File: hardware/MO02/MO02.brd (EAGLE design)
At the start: 49 x 24.5 mm, 33 parts, among them J1 AUDIO-JACK2PTH, J2 M04X2, Q1 G2XX3---PW20, Q4 32.768 kHz, SW1 DTS-6

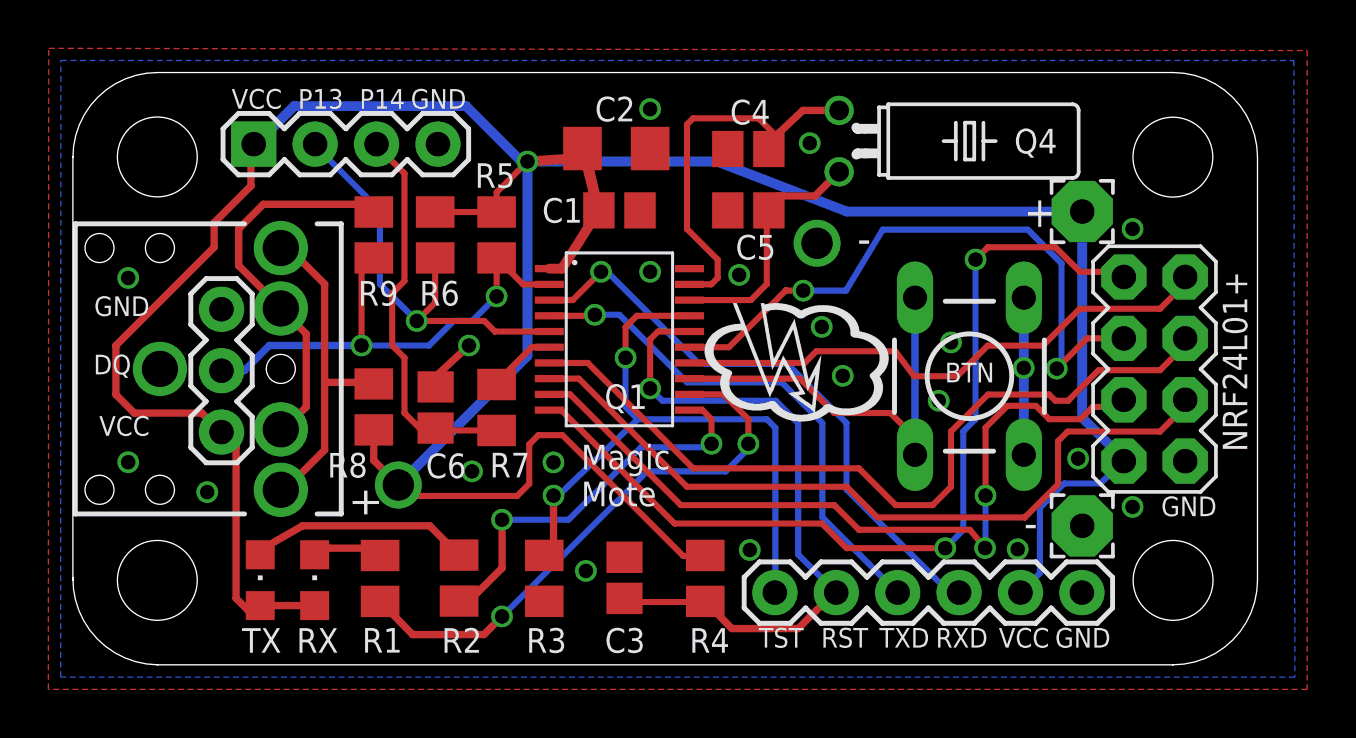
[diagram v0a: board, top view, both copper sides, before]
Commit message: 2x6mm watch crystal, isolated ground plane, no external caps
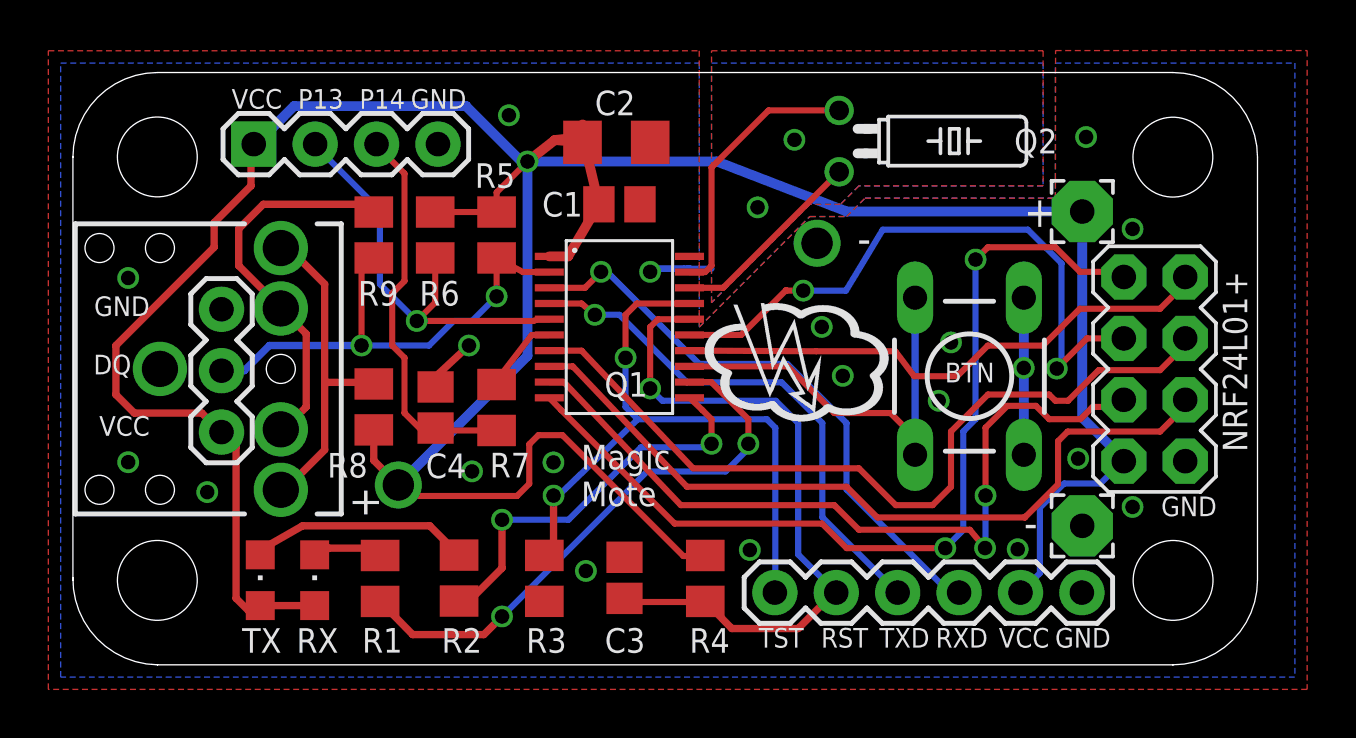
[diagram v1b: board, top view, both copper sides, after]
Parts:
- removed C5: 12nF, resistor:C0805
- removed C6: 330nF, resistor:C0805
- removed Q4: 32.768 kHz, crystal:TC38H
- added Q2: 32.768 kHz, crystal:TC26H
- C4: value 12nF -> 330nF
- moved C4 16.8 mm to (15.0, 10.6), turned to 90 degrees
- moved Q1 0.51 mm to (22.6, 14.0)
- moved C1 0.25 mm to (22.6, 19.1)
- moved C2 0.25 mm to (22.5, 21.6)
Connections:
- net GND: no longer C5.2, C6.2
- net N$7: now also C4.1; no longer C6.1
- net P2.6: now also Q2.1; no longer C4.1, Q4.1
- net P2.7: now also Q2.2; no longer C5.1, Q4.2
- net RXD: now also J4.4, Q1.3; no longer J4.3, Q1.4
- net TXD: now also J4.3, Q1.4; no longer J4.4, Q1.3
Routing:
- net P2.6: track 15.9 -> 11.3 mm
- net GND: track 8.87 -> 13.0 mm, vias 21 -> 22
- net TXD: track 24.5 -> 21.6 mm
- net +3V3: track 137.9 -> 135.1 mm
- net RXD: track 21.9 -> 24.3 mm
- net P2.7: track 10.2 -> 8.18 mm
- net RST: track 28.1 -> 28.6 mm
- net TST: track 27.3 -> 27.8 mm

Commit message: removed pulldown resistor on TST
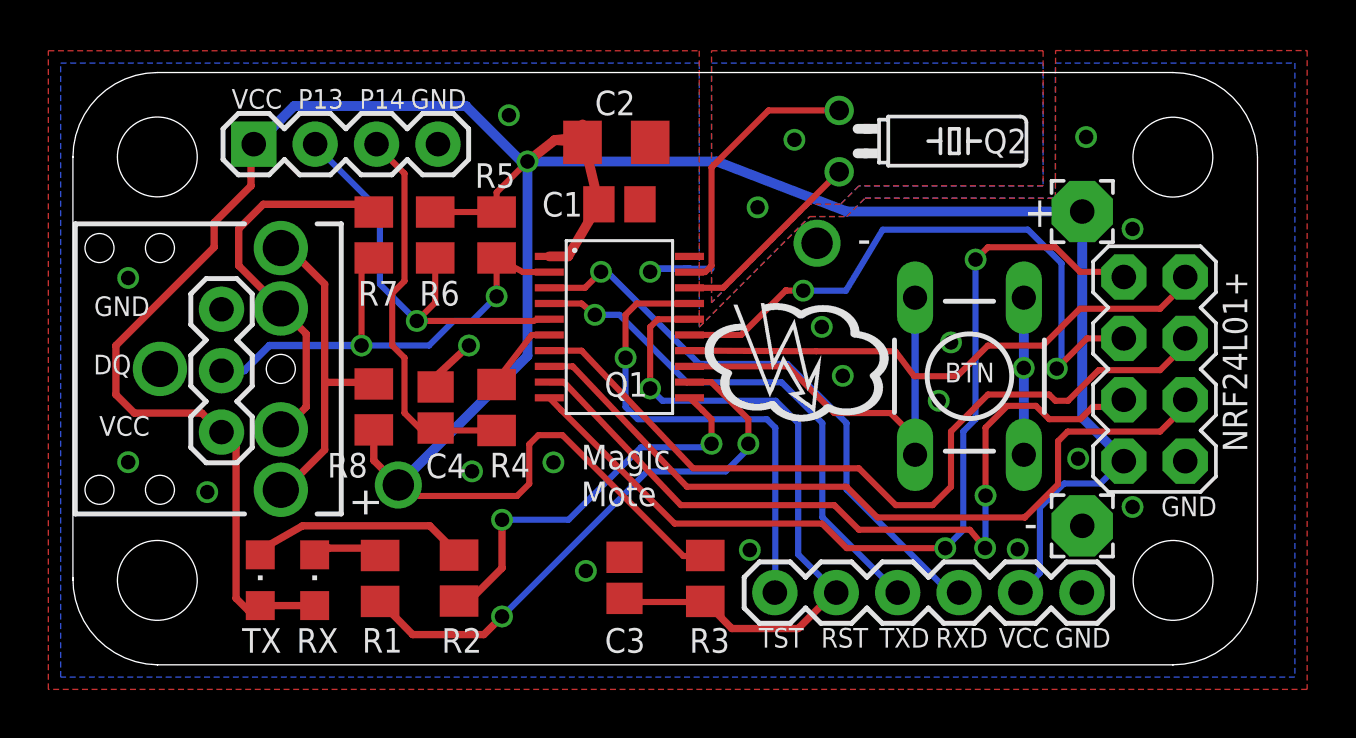
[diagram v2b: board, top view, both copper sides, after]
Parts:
- removed R9: 220R, resistor:M0805
- R4: value 47K -> 10K
- R7: value 10K -> 220R
- moved R4 11.2 mm to (17.5, 10.6), turned to 90 degrees
- moved R7 8.76 mm to (12.4, 17.8)
- moved R3 6.66 mm to (26.2, 3.57)
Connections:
- net +3V3: now also R3.1; no longer R4.1
- net DQ: now also R7.1; no longer R9.1
- net GND: no longer R3.2
- net N$4: now also R7.2; no longer R9.2
- net N$7: now also R4.1; no longer R7.1
- net P1.4: now also R4.2; no longer R7.2
- net RST: now also R3.2; no longer R4.2
- net TST: no longer R3.1
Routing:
- net TST: track 27.8 -> 20.0 mm, vias 2 -> 1
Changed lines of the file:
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@@
 <attribute name="MF" value="" x="31.695" y="21.663" size="1.778" layer="27" rot="R270" display="off"/>
 <attribute name="OC_FARNELL" value="unknown" x="31.695" y="21.663" size="1.778" layer="27" rot="R270" display="off"/>
-<attribute name="NAME" x="38.934" y="21.155" size="1.016" layer="25" font="vector" ratio="15"/>
+<attribute name="NAME" x="37.664" y="21.155" size="1.016" layer="25" font="vector" ratio="15"/>
 </element>
 <element name="J3" library="SparkFun" package="1X04" value="" x="7.4796" y="21.537" smashed="yes"/>
@@
 <attribute name="NAME" x="22" y="0.5" size="1.016" layer="25" font="vector" ratio="15"/>
 </element>
-<element name="R4" library="resistor" package="M0805" value="47K" x="26.158" y="3.5734" smashed="yes" rot="R270">
+<element name="R3" library="resistor" package="M0805" value="47K" x="26.158" y="3.5734" smashed="yes" rot="R270">
 <attribute name="RESISTANCE" value="4K7" x="26.158" y="3.5734" size="1.778" layer="27" rot="R270" display="off"/>
 <attribute name="NAME" x="25.5" y="0.5" size="1.016" layer="25" font="vector" ratio="15"/>
@@
 <element name="U$4" library="SparkFun" package="STAND-OFF" value="" x="3.492" y="21.008"/>
 <element name="U$5" library="SparkFun" package="STAND-OFF" value="" x="45.5" y="21" smashed="yes"/>
-<element name="R3" library="resistor" package="M0805" value="47K" x="19.5" y="3.5762" smashed="yes" rot="R270">
-<attribute name="RESISTANCE" value="4K7" x="19.5" y="3.5762" size="1.778" layer="27" rot="R270" display="off"/>
-<attribute name="NAME" x="18.75" y="0.5" size="1.016" layer="25" ratio="15"/>
-</element>
 <element name="-" library="wirepad" package="2,54/1,0" value="" x="41.75" y="5.75" smashed="yes">
 <attribute name="NAME" x="39.337" y="5.242" size="1.27" layer="25" ratio="15"/>
@@
 <attribute name="NAME" x="16.272" y="8.739" size="1.016" layer="25" font="vector" ratio="15" rot="R180"/>
 </element>
-<element name="R7" library="resistor" package="M0805" value="10K" x="17.526" y="10.644" smashed="yes" rot="R90">
+<element name="R4" library="resistor" package="M0805" value="10K" x="17.526" y="10.644" smashed="yes" rot="R90">
 <attribute name="RESISTANCE" value="4K7" x="17.526" y="10.644" size="1.778" layer="27" rot="R90" display="off"/>
 <attribute name="NAME" x="18.913" y="8.77" size="1.016" layer="25" font="vector" ratio="15" rot="R180"/>
@@
 <attribute name="NAME" x="12.192" y="8.763" size="1.016" layer="25" ratio="15" rot="R180"/>
 </element>
-<element name="R9" library="resistor" package="M0805" value="220R" x="12.446" y="17.78" smashed="yes" rot="R90">
+<element name="R7" library="resistor" package="M0805" value="220R" x="12.446" y="17.78" smashed="yes" rot="R90">
 <attribute name="RESISTANCE" value="4K7" x="12.446" y="17.78" size="1.778" layer="27" rot="R90" display="off"/>
 <attribute name="NAME" x="13.462" y="15.875" size="1.016" layer="25" ratio="15" rot="R180"/>
@@
 <contactref element="R5" pad="2"/>
 <contactref element="Q1" pad="2"/>
-<contactref element="R9" pad="1"/>
+<contactref element="R7" pad="1"/>
 <contactref element="J5" pad="2"/>
 <wire x1="19.7059" y1="16.2449" x2="18.6191" y2="16.2449" width="0.254" layer="1"/>
@@
 <contactref element="J2" pad="2"/>
 <contactref element="J3" pad="1"/>
-<contactref element="R4" pad="1"/>
+<contactref element="R3" pad="1"/>
 <contactref element="J4" pad="5"/>
 <contactref element="R6" pad="1"/>
@@
 <contactref element="Q1" pad="16"/>
 <contactref element="J4" pad="2"/>
-<contactref element="R4" pad="2"/>
+<contactref element="R3" pad="2"/>
 <contactref element="C3" pad="1"/>
 <wire x1="25.506" y1="14.295" x2="24.201" y2="14.295" width="0.254" layer="1"/>
@@
 <contactref element="Q1" pad="17"/>
 <contactref element="J4" pad="1"/>
-<contactref element="R3" pad="1"/>
 <wire x1="25.506" y1="14.945" x2="23.327" y2="14.945" width="0.254" layer="1"/>
 <wire x1="23.327" y1="14.945" x2="22.86" y2="14.478" width="0.254" layer="1"/>
@@
 <wire x1="29.0562" y1="9.8058" x2="29.0562" y2="3.0072" width="0.254" layer="16"/>
 <wire x1="29.0562" y1="3.0072" x2="29.0362" y2="2.9872" width="0.254" layer="16"/>
-<wire x1="19.5" y1="4.5262" x2="19.5122" y2="4.5262" width="0.3048" layer="1"/>
-<wire x1="19.5122" y1="4.5262" x2="19.812" y2="4.826" width="0.3048" layer="1"/>
-<via x="19.881" y="7" extent="1-16" drill="0.6" shape="square" alwaysstop="yes"/>
-<wire x1="19.881" y1="7" x2="20.081" y2="7" width="0.254" layer="16"/>
-<wire x1="20.081" y1="7" x2="23.368" y2="10.16" width="0.254" layer="16"/>
+<wire x1="19.881" y1="7" x2="20.081" y2="7" width="0" layer="19" extent="1-16"/>
+<wire x1="20.081" y1="7" x2="23.368" y2="10.16" width="0" layer="19" extent="1-16"/>
 <wire x1="22.86" y1="10.668" x2="23.368" y2="10.16" width="0.254" layer="16"/>
-<wire x1="19.881" y1="7" x2="19.881" y2="5.0342" width="0.3048" layer="1"/>
-<wire x1="19.881" y1="5.0342" x2="19.5" y2="4.5262" width="0.3048" layer="1"/>
+<wire x1="19.881" y1="7" x2="19.881" y2="5.0342" width="0" layer="19" extent="1-16"/>
 </signal>
 <signal name="TXD">
@@
 <signal name="P1.4">
 <contactref element="Q1" pad="6"/>
-<contactref element="R7" pad="2"/>
+<contactref element="R4" pad="2"/>
 <wire x1="19.7059" y1="13.645" x2="18.979" y2="13.645" width="0.254" layer="1"/>
 <wire x1="18.979" y1="13.645" x2="17.272" y2="11.43" width="0.254" layer="1"/>
@@
 <vertex x="-0.508" y="-0.508"/>
 </polygon>
-<contactref element="R3" pad="2"/>
 <via x="2.286" y="8.382" extent="1-16" drill="0.6" shape="square" alwaysstop="yes"/>
 <via x="2.286" y="16.002" extent="1-16" drill="0.6" shape="square" alwaysstop="yes"/>
@@
 <wire x1="24.0069" y1="16.3869" x2="24.003" y2="16.383" width="0.254" layer="16"/>
 <wire x1="24.003" y1="16.383" x2="23.876" y2="16.256" width="0.254" layer="16"/>
+<wire x1="43.831" y1="18.03" x2="41.91" y2="21.832" width="0" layer="19" extent="1-1"/>
+<wire x1="39.334" y1="15.188" x2="43.831" y2="18.03" width="0" layer="19" extent="1-1"/>
+<wire x1="41.581" y1="8.53" x2="39.37" y2="8.652" width="0" layer="19" extent="16-16"/>
+<wire x1="41.75" y1="5.75" x2="41.581" y2="8.53" width="0" layer="19" extent="1-1"/>
+<wire x1="43.831" y1="6.53" x2="41.75" y2="5.75" width="0" layer="19" extent="1-1"/>
+<wire x1="41.7362" y1="2.9872" x2="41.75" y2="5.75" width="0" layer="19" extent="1-1"/>
+<wire x1="39.081" y1="4.78" x2="41.75" y2="5.75" width="0" layer="19" extent="1-1"/>
+<wire x1="46.01" y1="8.423" x2="43.831" y2="6.53" width="0" layer="19" extent="1-1"/>
+<wire x1="39.331" y1="12.28" x2="39.334" y2="15.188" width="0" layer="19" extent="1-1"/>
+<wire x1="36.322" y1="13.335" x2="39.331" y2="12.28" width="0" layer="19" extent="1-1"/>
+<wire x1="35.814" y1="10.922" x2="36.322" y2="13.335" width="0" layer="19" extent="1-1"/>
+<wire x1="31.845" y1="11.953" x2="35.814" y2="10.922" width="0" layer="19" extent="1-1"/>
+<wire x1="30.976" y1="13.978" x2="31.845" y2="11.953" width="0" layer="19" extent="1-1"/>
+<wire x1="30.782" y1="17.438" x2="30.976" y2="13.978" width="0" layer="19" extent="1-1"/>
+<wire x1="28.321" y1="18.923" x2="30.782" y2="17.438" width="0" layer="19" extent="1-1"/>
+<wire x1="29.845" y1="21.717" x2="28.321" y2="18.923" width="0" layer="19" extent="1-1"/>
+<wire x1="26.416" y1="16.383" x2="28.321" y2="18.923" width="0" layer="19" extent="16-16"/>
+<wire x1="25.506" y1="16.8949" x2="25.5099" y2="16.383" width="0" layer="19" extent="1-16"/>
+<wire x1="23.456" y1="19.05" x2="24.0069" y2="16.3869" width="0" layer="19" extent="1-16"/>
+<wire x1="23.879" y1="21.61" x2="23.456" y2="19.05" width="0" layer="19" extent="1-1"/>
+<wire x1="18.034" y1="22.733" x2="23.879" y2="21.61" width="0" layer="19" extent="1-1"/>
+<wire x1="15.0996" y1="21.537" x2="18.034" y2="22.733" width="0" layer="19" extent="1-1"/>
+<wire x1="16.383" y1="13.208" x2="23.876" y2="16.256" width="0" layer="19" extent="1-1"/>
+<wire x1="16.51" y1="8.001" x2="15.002" y2="11.494" width="0" layer="19" extent="1-1"/>
+<wire x1="19.877" y1="8.373" x2="16.51" y2="8.001" width="0" layer="19" extent="1-1"/>
+<wire x1="21.219" y1="3.884" x2="19.877" y2="8.373" width="0" layer="19" extent="1-1"/>
+<wire x1="22.816" y1="4.4488" x2="21.219" y2="3.884" width="0" layer="19" extent="1-1"/>
+<wire x1="28" y1="4.75" x2="22.816" y2="4.4488" width="0" layer="19" extent="1-1"/>
+<wire x1="6.1468" y1="14.7066" x2="15.002" y2="11.922" width="0" layer="19" extent="1-1"/>
+<wire x1="3.6" y1="12.24" x2="6.1468" y2="14.7066" width="0" layer="19" extent="1-1"/>
+<wire x1="2.286" y1="16.002" x2="3.6" y2="12.24" width="0" layer="19" extent="1-1"/>
+<wire x1="2.286" y1="8.382" x2="3.6" y2="12.24" width="0" layer="19" extent="1-1"/>
+<wire x1="5.556" y1="7.144" x2="2.286" y2="8.382" width="0" layer="19" extent="1-1"/>
 </signal>
 <signal name="N$7">
 <contactref element="C4" pad="1"/>
-<contactref element="R7" pad="1"/>
+<contactref element="R4" pad="1"/>
 <contactref element="J3" pad="3"/>
 <wire x1="17.526" y1="9.694" x2="15.102" y2="9.694" width="0.254" layer="1"/>
@@
 <contactref element="J1" pad="RSH"/>
 <contactref element="J1" pad="TSH"/>
-<contactref element="R9" pad="2"/>
+<contactref element="R7" pad="2"/>
 <wire x1="8.6" y1="9.74" x2="8.724" y2="9.74" width="0.3048" layer="1"/>
 <wire x1="8.724" y1="9.74" x2="9.652" y2="10.668" width="0.3048" layer="1"/>

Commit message: 2x3 programming/serial header, SMD switch at side of board
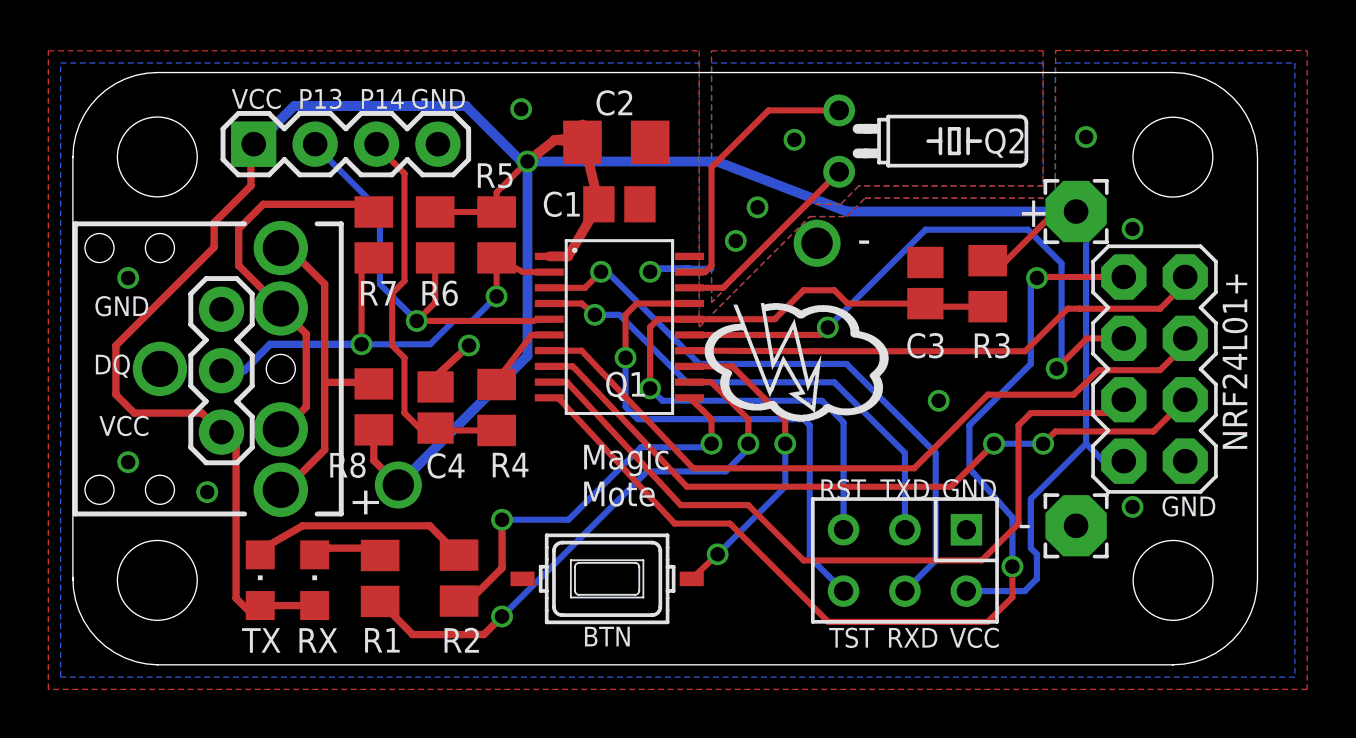
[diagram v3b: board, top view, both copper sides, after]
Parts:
- J4: value (none) -> CON_HEADER_2X03-PTH; device SparkFun:1X06 -> dp_devices:M2X3
- SW1: value DTS-6 -> SW_TACT_2P-3X6; device switch-tact:DTS-6 -> dp_devices:SW_TACT_3X6
- moved C3 17.4 mm to (35.3, 15.8)
- moved SW1 17.2 mm to (22.1, 3.56), turned to 180 degrees
- moved R3 16.9 mm to (37.8, 15.8)
- moved J4 5.54 mm to (34.4, 4.32), turned to 180 degrees
- moved + 0.25 mm to (41.5, 18.8)
- moved - 0.25 mm to (41.5, 5.75)
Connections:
- net +3V3: now also J4.2; no longer J4.5
- net BUTTON: no longer SW1.2
- net GND: now also J4.1, SW1.2; no longer J4.6, SW1.3, SW1.4
- net RST: now also J4.5; no longer J4.2
- net TST: now also J4.6; no longer J4.1
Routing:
- net +3V3: track 135.1 -> 124.6 mm
- net GND: track 13.0 -> 6.43 mm, vias 22 -> 13
- net BUTTON: track 19.0 -> 13.1 mm, vias 0 -> 2
- net IRQ: track 38.2 -> 42.2 mm
- net SCLK: track 33.6 -> 30.8 mm
- net CE: track 32.2 -> 29.9 mm, vias 0 -> 2
- net TST: track 20.0 -> 22.0 mm
- net RST: track 28.6 -> 30.4 mm
- net RXD: track 24.3 -> 25.6 mm
- net TXD: track 21.6 -> 20.4 mm
- net MISO: track 22.9 -> 21.9 mm
- net CSN: track 32.8 -> 32.1 mm, vias 2 -> 0
